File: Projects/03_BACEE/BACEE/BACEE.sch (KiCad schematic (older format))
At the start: 0 parts

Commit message: Create new child sheet and added project symbols
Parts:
- added BT?: Battery, symbol Device:Battery
- added C? (x2): C, symbol Device:C
- added C?: CP, symbol Device:CP
- added D?: LED, symbol Device:LED
- added R? (x2): R, symbol Device:R
- added U?: 24LC1025, symbol Memory_EEPROM:24LC1025
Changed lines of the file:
@@
 $Descr A4 11693 8268
 encoding utf-8
-Sheet 1 1
+Sheet 1 2
 Title "Battery-Powered Arduino Clone With Clock and External EEPROM"
 Date "2022-01-02"
@@
 Comment4 ""
 $EndDescr
+$Comp
+L Device:Battery BT?
+U 1 1 61D22E5D
+P 3000 3000
+F 0 "BT?" H 3108 3046 50  0000 L CNN
+F 1 "Battery" H 3108 2955 50  0000 L CNN
+F 2 "" V 3000 3060 50  0001 C CNN
+F 3 "~" V 3000 3060 50  0001 C CNN
+	1    3000 3000
+	1    0    0    -1
+$EndComp
+$Comp
+L Device:LED D?
+U 1 1 61D23F53
+P 3000 3550
+F 0 "D?" H 2993 3767 50  0000 C CNN
+F 1 "LED" H 2993 3676 50  0000 C CNN
+F 2 "" H 3000 3550 50  0001 C CNN
+F 3 "~" H 3000 3550 50  0001 C CNN
+	1    3000 3550
+	1    0    0    -1
+$EndComp
+$Comp
+L Device:C C?
+U 1 1 61D244B0
+P 3850 2700
+F 0 "C?" H 3965 2746 50  0000 L CNN
+F 1 "C" H 3965 2655 50  0000 L CNN
+F 2 "" H 3888 2550 50  0001 C CNN
+F 3 "~" H 3850 2700 50  0001 C CNN
+	1    3850 2700
+	1    0    0    -1
+$EndComp
+$Comp
+L Device:C C?
+U 1 1 61D24B04
+P 3850 3250
+F 0 "C?" H 3965 3296 50  0000 L CNN
+F 1 "C" H 3965 3205 50  0000 L CNN
+F 2 "" H 3888 3100 50  0001 C CNN
+F 3 "~" H 3850 3250 50  0001 C CNN
+	1    3850 3250
+	1    0    0    -1
+$EndComp
+$Comp
+L Device:CP C?
+U 1 1 61D25462
+P 3850 3800
+F 0 "C?" H 3968 3846 50  0000 L CNN
+F 1 "CP" H 3968 3755 50  0000 L CNN
+F 2 "" H 3888 3650 50  0001 C CNN
+F 3 "~" H 3850 3800 50  0001 C CNN
+	1    3850 3800
+	1    0    0    -1
+$EndComp
+$Comp
+L Device:R R?
+U 1 1 61D25BF7
+P 4650 2700
+F 0 "R?" H 4720 2746 50  0000 L CNN
+F 1 "R" H 4720 2655 50  0000 L CNN
+F 2 "" V 4580 2700 50  0001 C CNN
+F 3 "~" H 4650 2700 50  0001 C CNN
+	1    4650 2700
+	1    0    0    -1
+$EndComp
+$Comp
+L Device:R R?
+U 1 1 61D26130
+P 4650 3250
+F 0 "R?" H 4720 3296 50  0000 L CNN
+F 1 "R" H 4720 3205 50  0000 L CNN
+F 2 "" V 4580 3250 50  0001 C CNN
+F 3 "~" H 4650 3250 50  0001 C CNN
+	1    4650 3250
+	1    0    0    -1
+$EndComp
+$Comp
+L Memory_EEPROM:24LC1025 U?
+U 1 1 61D26D32
+P 5750 2950
+F 0 "U?" H 5750 3431 50  0000 C CNN
+F 1 "24LC1025" H 5750 3340 50  0000 C CNN
+F 2 "" H 5750 2950 50  0001 C CNN
+F 3 "http://ww1.microchip.com/downloads/en/DeviceDoc/21941B.pdf" H 5750 2950 50  0001 C CNN
+	1    5750 2950
+	1    0    0    -1
+$EndComp
+$Sheet
+S 5350 3600 1650 2150
+U 61D27AD2
+F0 "Connectors" 50
+F1 "Connectors.sch" 50
+$EndSheet
 $EndSCHEMATC

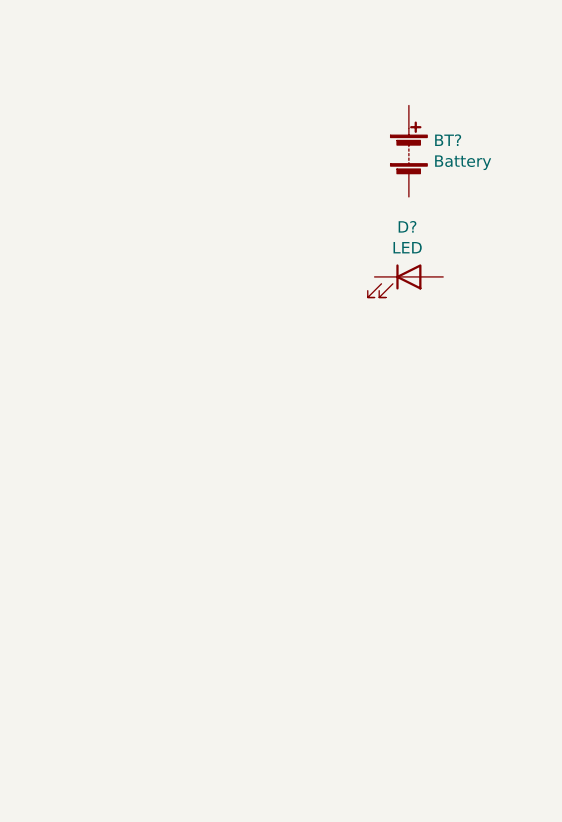
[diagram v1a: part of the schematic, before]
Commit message: Project 3: Add symbol for Atmega328P-AU onto schematic
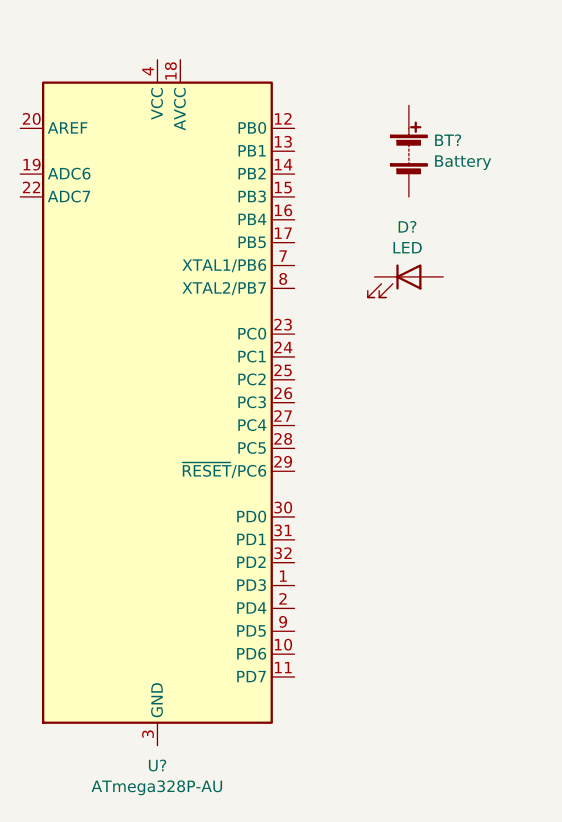
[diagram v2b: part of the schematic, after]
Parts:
- added U?: ATmega328P-AU, Package_QFP:TQFP-32_7x7mm_P0.8mm, symbol MCU_Microchip_ATmega:ATmega328P-AU
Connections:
- new net: U?.21 (GND), U?.3 (GND), U?.5 (GND)
- new net: U?.4 (VCC), U?.6 (VCC)
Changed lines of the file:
@@
 F1 "Connectors.sch" 50
 $EndSheet
+$Comp
+L MCU_Microchip_ATmega:ATmega328P-AU U?
+U 1 1 61D2E20A
+P 1900 4100
+F 0 "U?" H 1900 2511 50  0000 C CNN
+F 1 "ATmega328P-AU" H 1900 2420 50  0000 C CNN
+F 2 "Package_QFP:TQFP-32_7x7mm_P0.8mm" H 1900 4100 50  0001 C CIN
+F 3 "http://ww1.microchip.com/downloads/en/DeviceDoc/ATmega328_P%20AVR%20MCU%20with%20picoPower%20Technology%20Data%20Sheet%2040001984A.pdf" H 1900 4100 50  0001 C CNN
+	1    1900 4100
+	1    0    0    -1
+$EndComp
 $EndSCHEMATC

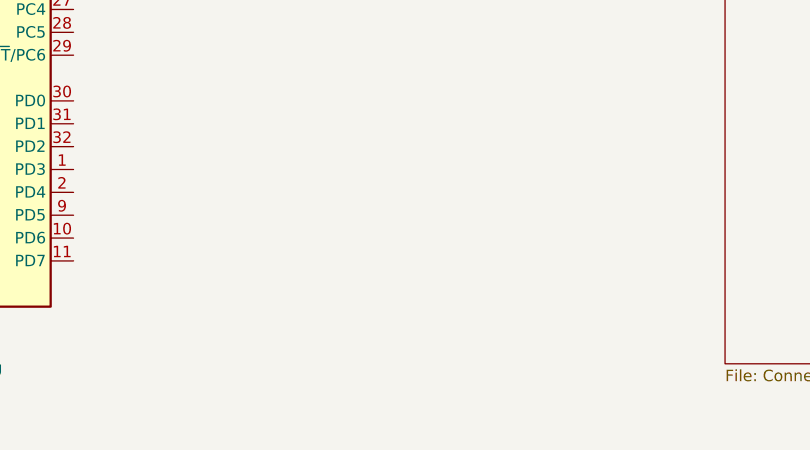
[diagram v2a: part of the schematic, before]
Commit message: Project 3: Add clock IC custom symbol
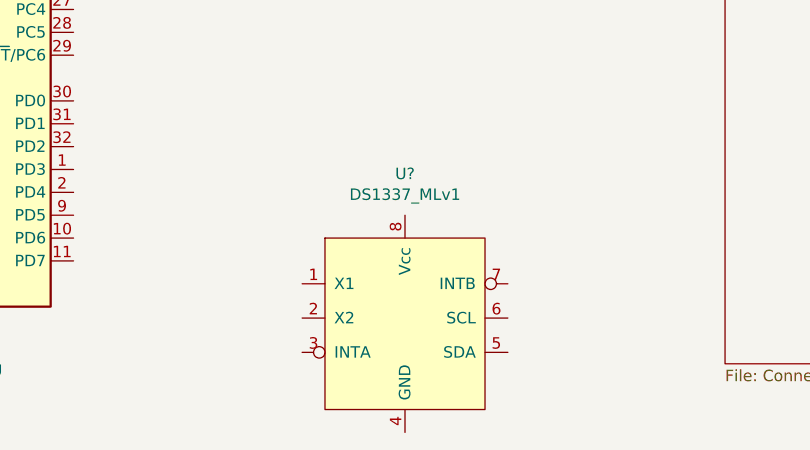
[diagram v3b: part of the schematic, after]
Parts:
- added U?: DS1337_MLv1, symbol Project3:DS1337_MLv1
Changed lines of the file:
@@
+	1    0    0    -1
+$EndComp
+$Comp
+L Project3:DS1337_MLv1 U?
+U 1 1 61D31649
+P 3950 5150
+F 0 "U?" H 3950 5381 50  0000 C CNN
+F 1 "DS1337_MLv1" H 3950 5290 50  0000 C CNN
+F 2 "" H 4250 5150 50  0001 C CNN
+F 3 "https://datasheets.maximintegrated.com/en/ds/DS1337-DS1337C.pdf" H 4250 5150 50  0001 C CNN
+	1    3950 5150
 	1    0    0    -1
 $EndComp

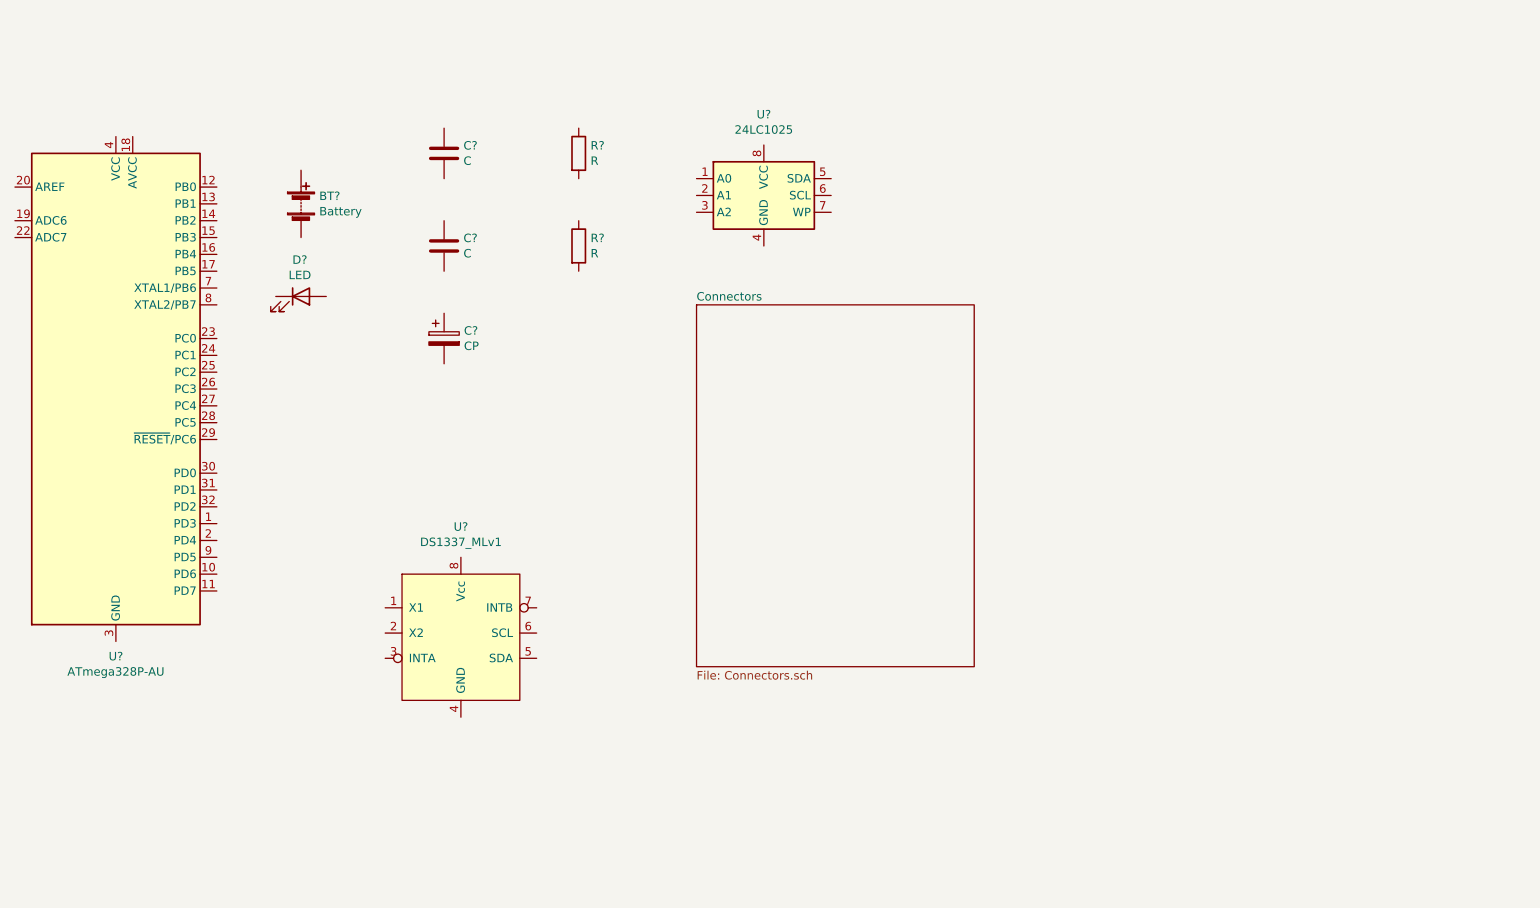
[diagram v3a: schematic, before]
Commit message: Project 3: Add another item to parts list/schematic - two 2-pin crystals
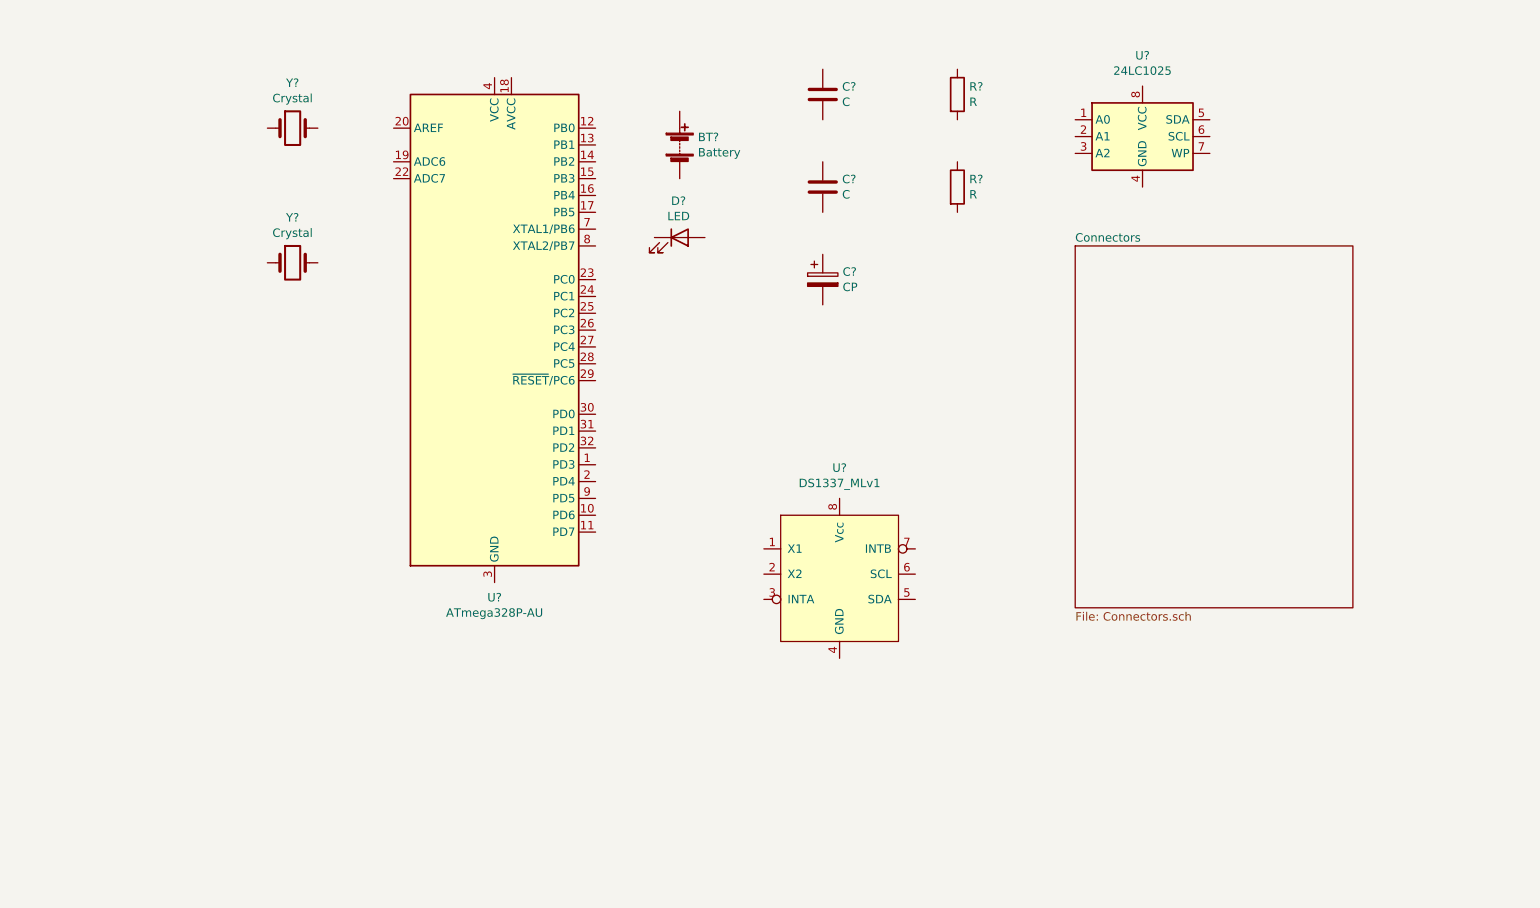
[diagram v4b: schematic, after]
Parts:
- added Y? (x2): Crystal, symbol Device:Crystal
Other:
- moved on the sheet: BT?, C?, D?, R?, U?
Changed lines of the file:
@@
 L Device:Battery BT?
 U 1 1 61D22E5D
-P 3000 3000
-F 0 "BT?" H 3108 3046 50  0000 L CNN
-F 1 "Battery" H 3108 2955 50  0000 L CNN
-F 2 "" V 3000 3060 50  0001 C CNN
-F 3 "~" V 3000 3060 50  0001 C CNN
-	1    3000 3000
+P 5250 2650
+F 0 "BT?" H 5358 2696 50  0000 L CNN
+F 1 "Battery" H 5358 2605 50  0000 L CNN
+F 2 "" V 5250 2710 50  0001 C CNN
+F 3 "~" V 5250 2710 50  0001 C CNN
+	1    5250 2650
 	1    0    0    -1
 $EndComp
@@
 L Device:LED D?
 U 1 1 61D23F53
-P 3000 3550
-F 0 "D?" H 2993 3767 50  0000 C CNN
-F 1 "LED" H 2993 3676 50  0000 C CNN
-F 2 "" H 3000 3550 50  0001 C CNN
-F 3 "~" H 3000 3550 50  0001 C CNN
-	1    3000 3550
+P 5250 3200
+F 0 "D?" H 5243 3417 50  0000 C CNN
+F 1 "LED" H 5243 3326 50  0000 C CNN
+F 2 "" H 5250 3200 50  0001 C CNN
+F 3 "~" H 5250 3200 50  0001 C CNN
+	1    5250 3200
 	1    0    0    -1
 $EndComp
@@
 L Device:C C?
 U 1 1 61D244B0
-P 3850 2700
-F 0 "C?" H 3965 2746 50  0000 L CNN
-F 1 "C" H 3965 2655 50  0000 L CNN
-F 2 "" H 3888 2550 50  0001 C CNN
-F 3 "~" H 3850 2700 50  0001 C CNN
-	1    3850 2700
+P 6100 2350
+F 0 "C?" H 6215 2396 50  0000 L CNN
+F 1 "C" H 6215 2305 50  0000 L CNN
+F 2 "" H 6138 2200 50  0001 C CNN
+F 3 "~" H 6100 2350 50  0001 C CNN
+	1    6100 2350
 	1    0    0    -1
 $EndComp
@@
 L Device:C C?
 U 1 1 61D24B04
-P 3850 3250
-F 0 "C?" H 3965 3296 50  0000 L CNN
-F 1 "C" H 3965 3205 50  0000 L CNN
-F 2 "" H 3888 3100 50  0001 C CNN
-F 3 "~" H 3850 3250 50  0001 C CNN
-	1    3850 3250
+P 6100 2900
+F 0 "C?" H 6215 2946 50  0000 L CNN
+F 1 "C" H 6215 2855 50  0000 L CNN
+F 2 "" H 6138 2750 50  0001 C CNN
+F 3 "~" H 6100 2900 50  0001 C CNN
+	1    6100 2900
 	1    0    0    -1
 $EndComp
@@
 L Device:CP C?
 U 1 1 61D25462
-P 3850 3800
-F 0 "C?" H 3968 3846 50  0000 L CNN
-F 1 "CP" H 3968 3755 50  0000 L CNN
-F 2 "" H 3888 3650 50  0001 C CNN
-F 3 "~" H 3850 3800 50  0001 C CNN
-	1    3850 3800
+P 6100 3450
+F 0 "C?" H 6218 3496 50  0000 L CNN
+F 1 "CP" H 6218 3405 50  0000 L CNN
+F 2 "" H 6138 3300 50  0001 C CNN
+F 3 "~" H 6100 3450 50  0001 C CNN
+	1    6100 3450
 	1    0    0    -1
 $EndComp
@@
 L Device:R R?
 U 1 1 61D25BF7
-P 4650 2700
-F 0 "R?" H 4720 2746 50  0000 L CNN
-F 1 "R" H 4720 2655 50  0000 L CNN
-F 2 "" V 4580 2700 50  0001 C CNN
-F 3 "~" H 4650 2700 50  0001 C CNN
-	1    4650 2700
+P 6900 2350
+F 0 "R?" H 6970 2396 50  0000 L CNN
+F 1 "R" H 6970 2305 50  0000 L CNN
+F 2 "" V 6830 2350 50  0001 C CNN
+F 3 "~" H 6900 2350 50  0001 C CNN
+	1    6900 2350
 	1    0    0    -1
 $EndComp
@@
 L Device:R R?
 U 1 1 61D26130
-P 4650 3250
-F 0 "R?" H 4720 3296 50  0000 L CNN
-F 1 "R" H 4720 3205 50  0000 L CNN
-F 2 "" V 4580 3250 50  0001 C CNN
-F 3 "~" H 4650 3250 50  0001 C CNN
-	1    4650 3250
+P 6900 2900
+F 0 "R?" H 6970 2946 50  0000 L CNN
+F 1 "R" H 6970 2855 50  0000 L CNN
+F 2 "" V 6830 2900 50  0001 C CNN
+F 3 "~" H 6900 2900 50  0001 C CNN
+	1    6900 2900
 	1    0    0    -1
 $EndComp
@@
 L Memory_EEPROM:24LC1025 U?
 U 1 1 61D26D32
-P 5750 2950
-F 0 "U?" H 5750 3431 50  0000 C CNN
-F 1 "24LC1025" H 5750 3340 50  0000 C CNN
-F 2 "" H 5750 2950 50  0001 C CNN
-F 3 "http://ww1.microchip.com/downloads/en/DeviceDoc/21941B.pdf" H 5750 2950 50  0001 C CNN
-	1    5750 2950
+P 8000 2600
+F 0 "U?" H 8000 3081 50  0000 C CNN
+F 1 "24LC1025" H 8000 2990 50  0000 C CNN
+F 2 "" H 8000 2600 50  0001 C CNN
+F 3 "http://ww1.microchip.com/downloads/en/DeviceDoc/21941B.pdf" H 8000 2600 50  0001 C CNN
+	1    8000 2600
 	1    0    0    -1
 $EndComp
 $Sheet
-S 5350 3600 1650 2150
+S 7600 3250 1650 2150
 U 61D27AD2
 F0 "Connectors" 50
@@
 L MCU_Microchip_ATmega:ATmega328P-AU U?
 U 1 1 61D2E20A
-P 1900 4100
-F 0 "U?" H 1900 2511 50  0000 C CNN
-F 1 "ATmega328P-AU" H 1900 2420 50  0000 C CNN
-F 2 "Package_QFP:TQFP-32_7x7mm_P0.8mm" H 1900 4100 50  0001 C CIN
-F 3 "http://ww1.microchip.com/downloads/en/DeviceDoc/ATmega328_P%20AVR%20MCU%20with%20picoPower%20Technology%20Data%20Sheet%2040001984A.pdf" H 1900 4100 50  0001 C CNN
-	1    1900 4100
+P 4150 3750
+F 0 "U?" H 4150 2161 50  0000 C CNN
+F 1 "ATmega328P-AU" H 4150 2070 50  0000 C CNN
+F 2 "Package_QFP:TQFP-32_7x7mm_P0.8mm" H 4150 3750 50  0001 C CIN
+F 3 "http://ww1.microchip.com/downloads/en/DeviceDoc/ATmega328_P%20AVR%20MCU%20with%20picoPower%20Technology%20Data%20Sheet%2040001984A.pdf" H 4150 3750 50  0001 C CNN
+	1    4150 3750
 	1    0    0    -1
 $EndComp
@@
 L Project3:DS1337_MLv1 U?
 U 1 1 61D31649
-P 3950 5150
-F 0 "U?" H 3950 5381 50  0000 C CNN
-F 1 "DS1337_MLv1" H 3950 5290 50  0000 C CNN
-F 2 "" H 4250 5150 50  0001 C CNN
-F 3 "https://datasheets.maximintegrated.com/en/ds/DS1337-DS1337C.pdf" H 4250 5150 50  0001 C CNN
-	1    3950 5150
+P 6200 4800
+F 0 "U?" H 6200 5031 50  0000 C CNN
+F 1 "DS1337_MLv1" H 6200 4940 50  0000 C CNN
+F 2 "" H 6500 4800 50  0001 C CNN
+F 3 "https://datasheets.maximintegrated.com/en/ds/DS1337-DS1337C.pdf" H 6500 4800 50  0001 C CNN
+	1    6200 4800
 	1    0    0    -1
 $EndComp
+$Comp
+L Device:Crystal Y?
+U 1 1 61D3267A
+P 2950 2550
+F 0 "Y?" H 2950 2818 50  0000 C CNN
+F 1 "Crystal" H 2950 2727 50  0000 C CNN
+F 2 "" H 2950 2550 50  0001 C CNN
+F 3 "~" H 2950 2550 50  0001 C CNN
+	1    2950 2550
+	1    0    0    -1
+$EndComp
+$Comp
+L Device:Crystal Y?
+U 1 1 61D331D7
+P 2950 3350
+F 0 "Y?" H 2950 3618 50  0000 C CNN
+F 1 "Crystal" H 2950 3527 50  0000 C CNN
+F 2 "" H 2950 3350 50  0001 C CNN
+F 3 "~" H 2950 3350 50  0001 C CNN
+	1    2950 3350
+	1    0    0    -1
+$EndComp
